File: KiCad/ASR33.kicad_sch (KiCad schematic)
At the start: 38 parts, among them J1 USB-C, J2 Conn_01x04, J3 Conn_01x05, Q1 NX7002AK, SW1 SW_Push, U1 ESP32-WROOM-32, U2 FT231XQ, U3 NCR402U, U4 NCR402U, U5 LMR16006+FB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

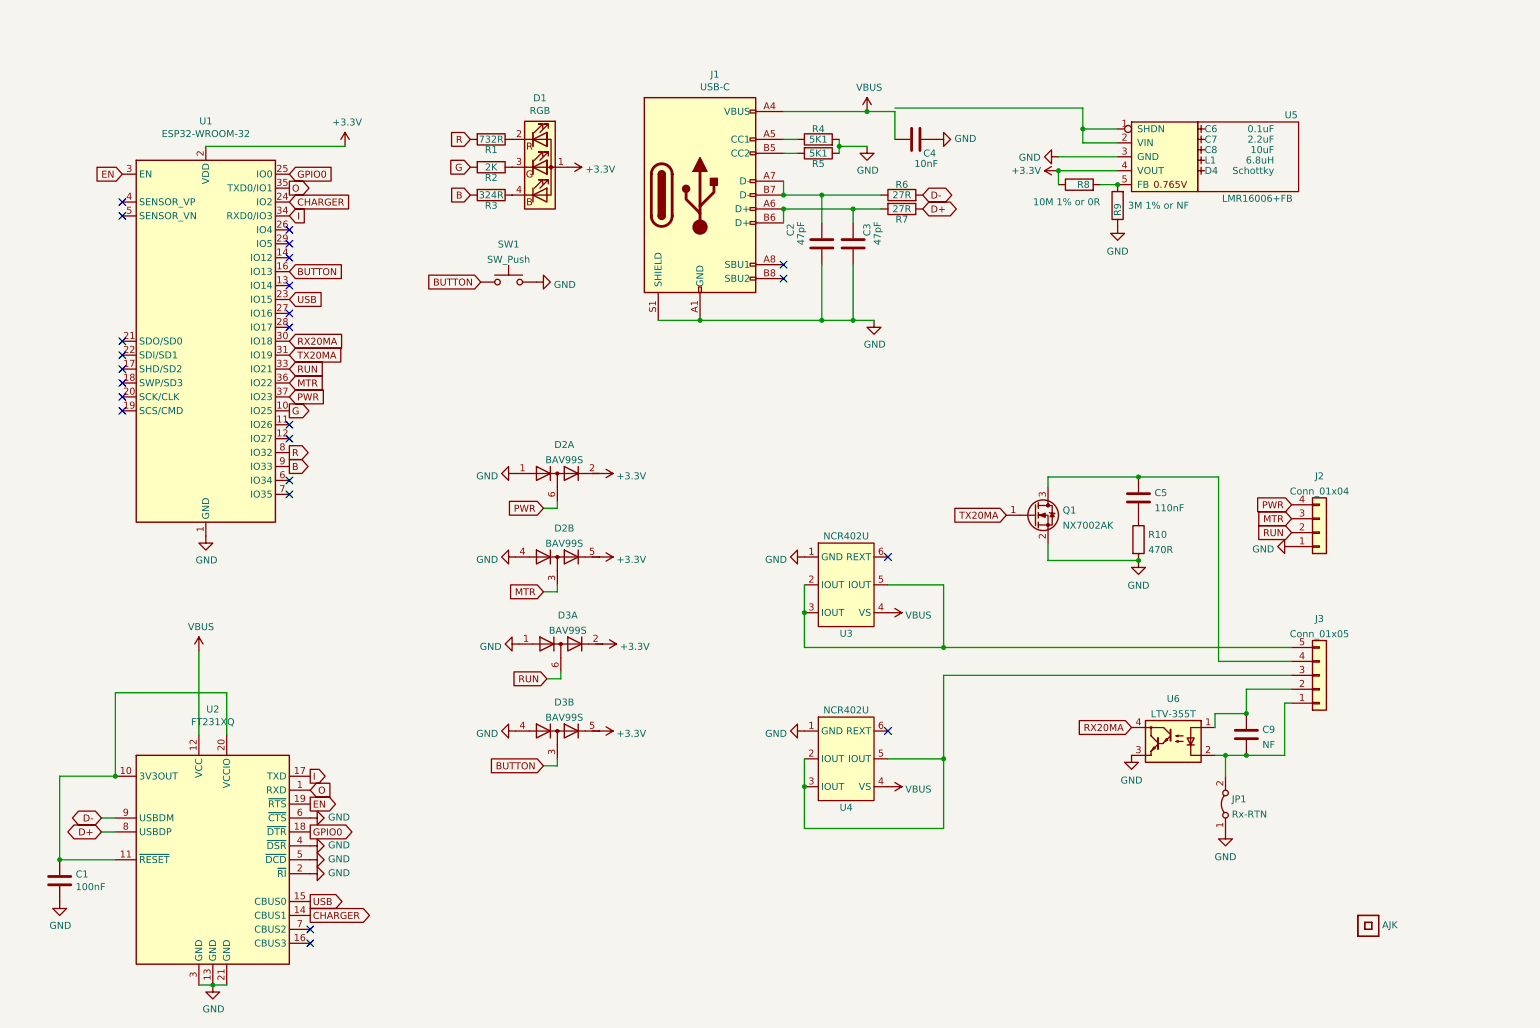
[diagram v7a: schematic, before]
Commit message: Complete re-work with more connectors.
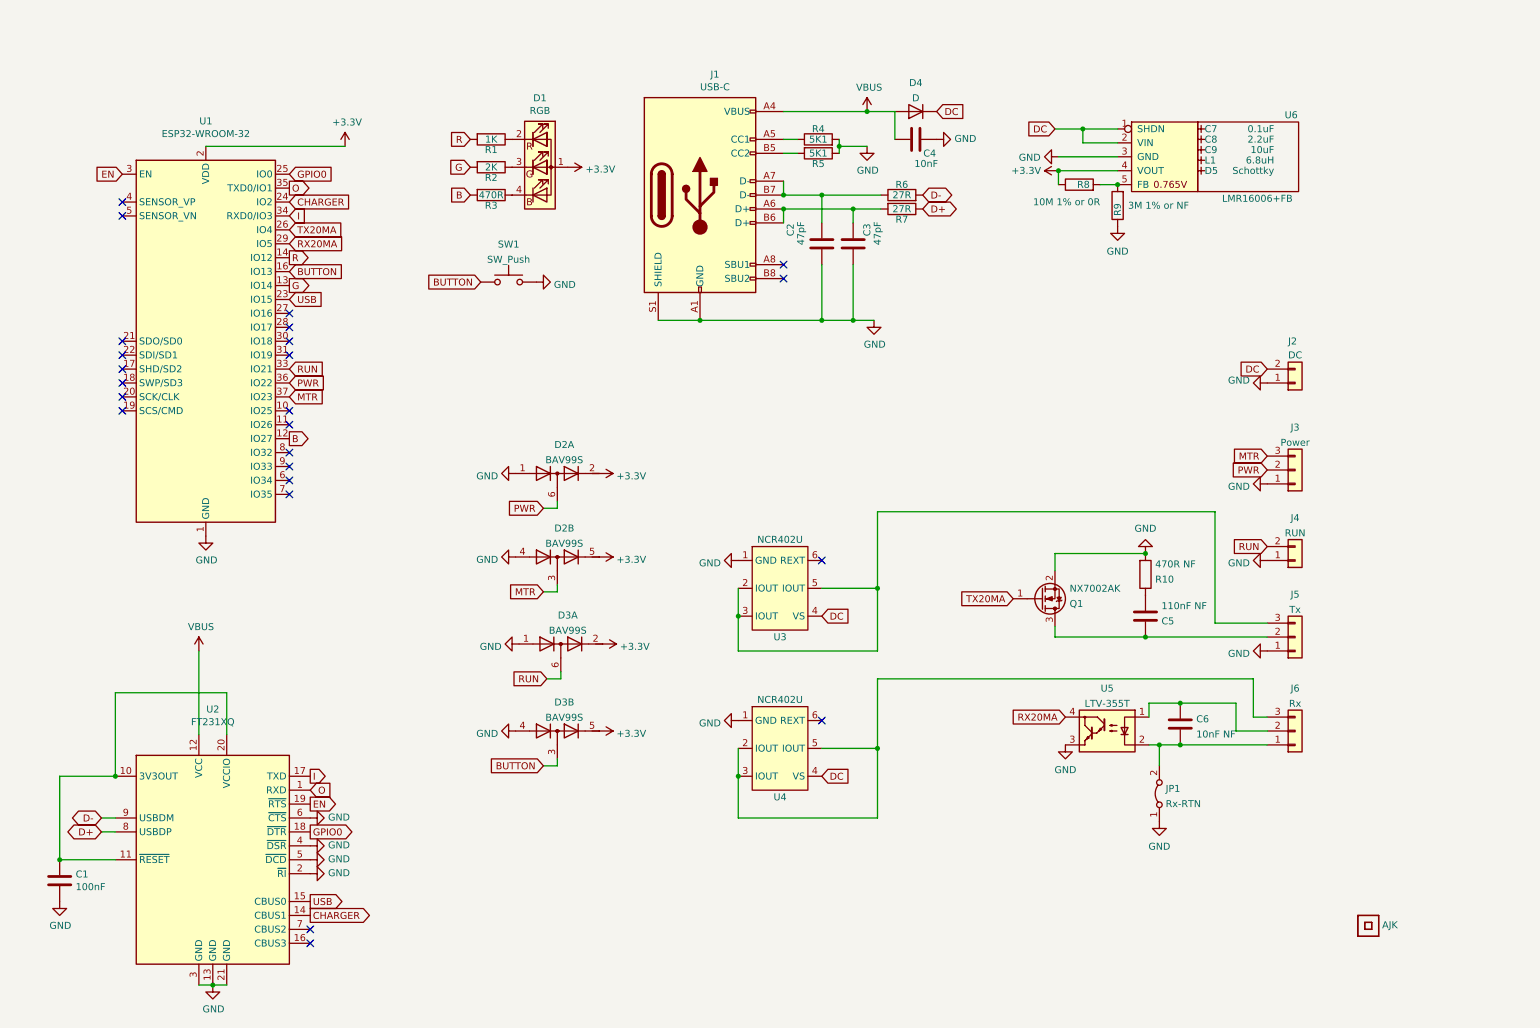
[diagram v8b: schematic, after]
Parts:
- removed J2: Conn_01x04, RevK:Molex_MiniSPOX_H4RA, symbol Connector_Generic:Conn_01x04
- removed J3: Conn_01x05, RevK:Molex_MiniSPOX_H5RA, symbol Connector_Generic:Conn_01x05
- added D4: D, Diode_SMD:D_1206_3216Metric, symbol Device:D
- added J2: DC, RevK:Molex_MiniSPOX_H2RA, symbol Connector_Generic:Conn_01x02
- added J3: Power, RevK:Molex_MiniSPOX_H3RA, symbol Connector_Generic:Conn_01x03
- added J4: RUN, RevK:Molex_MiniSPOX_H2RA, symbol Connector_Generic:Conn_01x02
- added J5: Tx, RevK:Molex_MiniSPOX_H3RA, symbol Connector_Generic:Conn_01x03
- added J6: Rx, RevK:Molex_MiniSPOX_H3RA, symbol Connector_Generic:Conn_01x03
- C5: value 110nF -> 110nF NF; now left out of the parts list
- C6: renamed from C9; value NF -> 10nF NF
- R1: value 732R -> 1K
- R10: value 470R -> 470R NF; now left out of the parts list
- R3: value 324R -> 470R
- renumbered C6 to C7, C7 to C8, C8 to C9, D4 to D5, U6 to U5, U5 to U6
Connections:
- net B: now also U1.12 (IO27); no longer U1.9 (IO33)
- net G: now also U1.13 (IO14); no longer U1.10 (IO25)
- net GND: now also J2.1 (Pin_1), J3.1 (Pin_1), J4.1 (Pin_1), J5.1 (Pin_1)
- net MTR: now also U1.37 (IO23), J3.3 (Pin_3); no longer U1.36 (IO22)
- net PWR: now also U1.36 (IO22), J3.2 (Pin_2); no longer U1.37 (IO23)
- net R: now also U1.14 (IO12); no longer U1.8 (IO32)
- net RUN: now also J4.2 (Pin_2)
- net RX20MA: now also U1.29 (IO5); no longer U1.30 (IO18)
- net TX20MA: now also U1.26 (IO4); no longer U1.31 (IO19)
- net VBUS: now also D4.2 (A); no longer U3.4 (VS), U4.4 (VS)
- net at C5.1, Q1.3 (D): now also J5.2 (Pin_2)
- net at C6.1, JP1.2 (B), U5.2: now also J6.1 (Pin_1)
- net at C6.2, U5.1: now also J6.2 (Pin_2)
- net at U4.2 (IOUT), U4.3 (IOUT), U4.5 (IOUT): now also J6.3 (Pin_3)
- net at U3.2 (IOUT), U3.3 (IOUT), U3.5 (IOUT): now also J5.3 (Pin_3)
- net DC: now reaches U6.1 (SHDN), U6.2 (VIN)
- net DC: now also U3.4 (VS), U4.4 (VS), D4.1 (K), J2.2 (Pin_2)
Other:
- moved on the sheet: C5, C6, JP1, Q1, R10, U3, U4, U5
